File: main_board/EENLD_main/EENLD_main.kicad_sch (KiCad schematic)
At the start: 17 parts, among them J101 Conn_01x06_Pin, J102 Conn_01x02_Pin, SW101 SW_Push, SW102 SW_SPDT, U101 Pico, U102 74HC595, U103 D198K

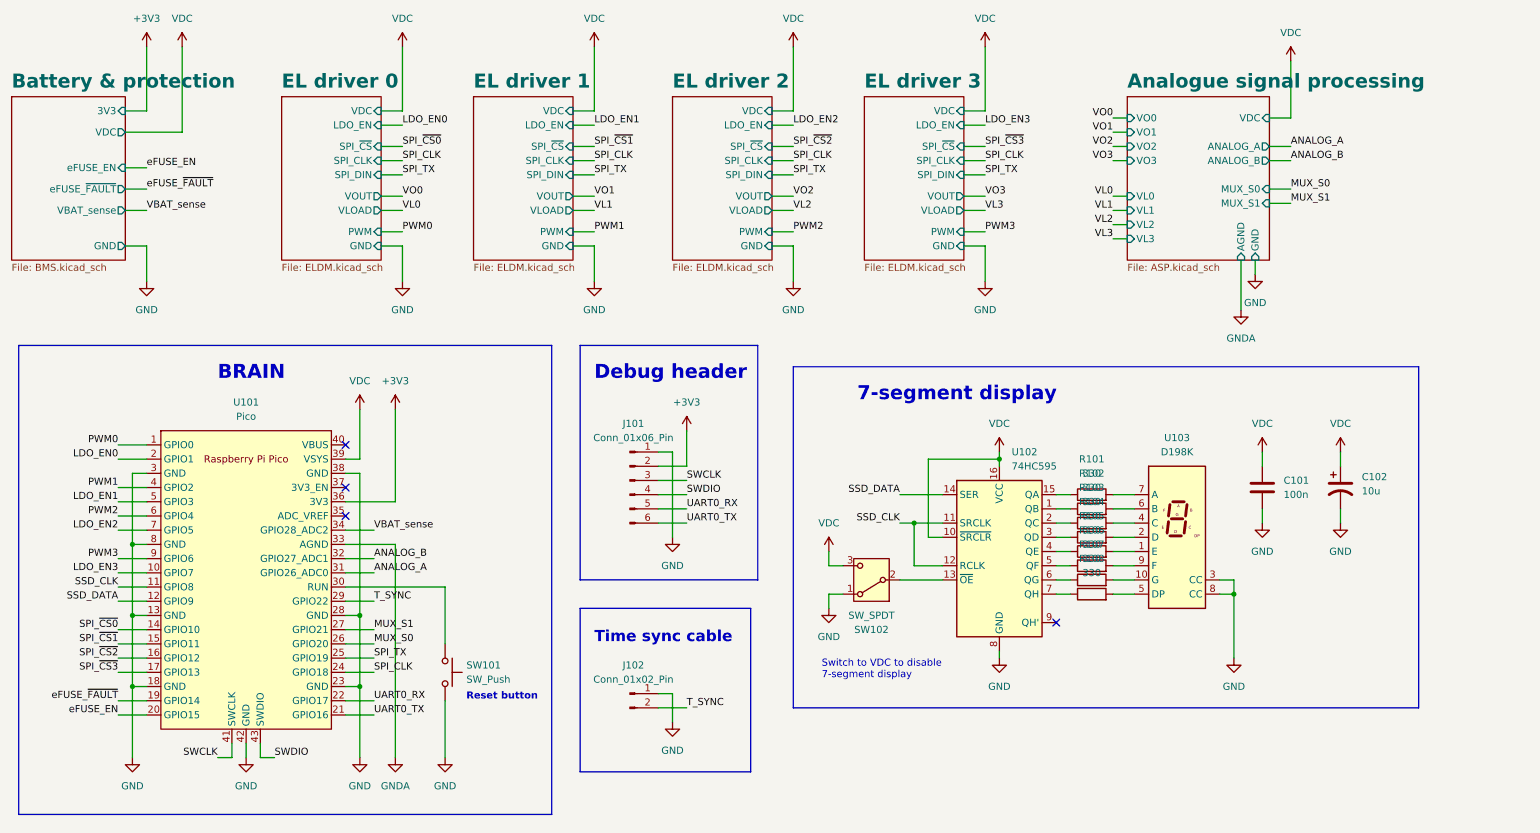
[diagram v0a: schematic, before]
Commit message: Finished PCB layout v0.1.
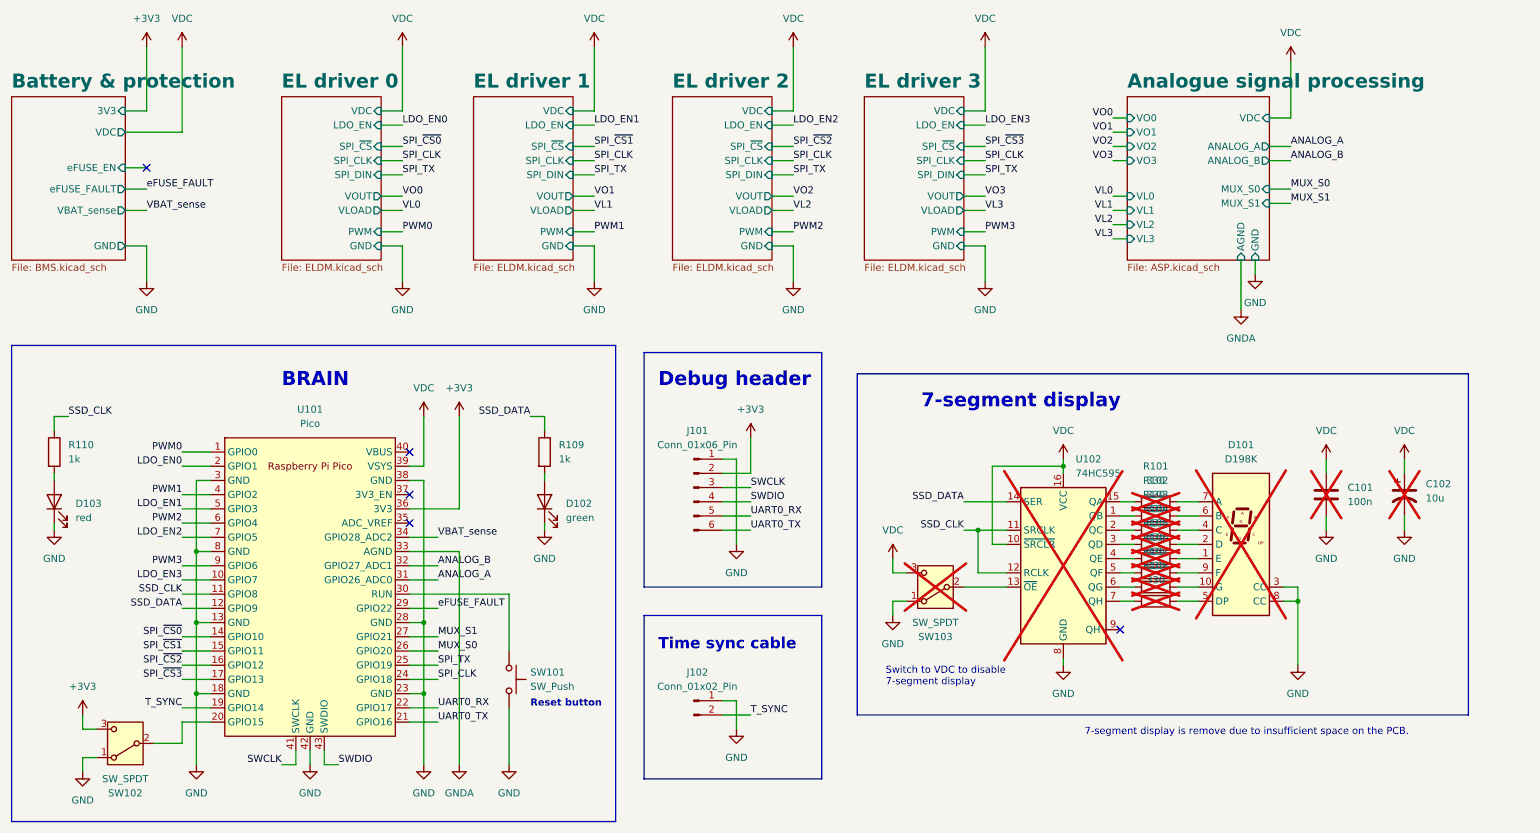
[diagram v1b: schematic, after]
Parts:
- added D102: green, LED_SMD:LED_0805_2012Metric_Pad1.15x1.40mm_HandSolder, symbol Device:LED
- added D103: red, LED_SMD:LED_0805_2012Metric_Pad1.15x1.40mm_HandSolder, symbol Device:LED
- added R109, R110: 1k, Resistor_SMD:R_0603_1608Metric_Pad0.98x0.95mm_HandSolder, symbol Device:R
- added SW102: SW_SPDT, Button_Switch_THT:SW_CK_JS202011CQN_DPDT_Straight, symbol Switch:SW_SPDT
- C101: footprint (none) -> Capacitor_SMD:C_0603_1608Metric_Pad1.08x0.95mm_HandSolder; LCSC (none) -> C14663; now not fitted; now left out of the parts list
- C102: footprint (none) -> Capacitor_THT:CP_Radial_D8.0mm_P2.50mm; now not fitted; now left out of the parts list
- D101: renamed from U103; now not fitted; now left out of the parts list
- J101: footprint (none) -> Connector_PinHeader_2.54mm:PinHeader_1x06_P2.54mm_Vertical
- J102: footprint (none) -> Connector_PinHeader_2.54mm:PinHeader_1x02_P2.54mm_Vertical
- R101, R102, R103, R104, R105, R106, R107, R108: footprint (none) -> Resistor_SMD:R_0603_1608Metric_Pad0.98x0.95mm_HandSolder; LCSC (none) -> C23138; now not fitted; now left out of the parts list
- SW101: footprint Button_Switch_THT:SW_PUSH_6mm -> Button_Switch_SMD:SW_Push_1P1T_NO_6x6mm_H9.5mm
- SW103: renamed from SW102; footprint (none) -> Button_Switch_THT:SW_CK_JS202011CQN_DPDT_Straight; now not fitted; now left out of the parts list
- U101: footprint RPi_Pico:RPi_Pico_SMD_TH -> More Pi Pico:RaspberryPi_Pico_Original_SMD
- U102: LCSC (none) -> C5947; now not fitted; now left out of the parts list
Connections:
- net eFUSE_~{FAULT} is gone; now on net T_SYNC: U101.19 (GPIO14)
- net +3V3: now also SW102.3 (C)
- net GND: now also D102.1 (K), D103.1 (K), SW102.1 (A)
- net SSD_CLK: now also R110.1
- net SSD_DATA: now also R109.1
- net T_SYNC: no longer U101.29 (GPIO22)
- net eFUSE_EN: no longer names the net of U101.20 (GPIO15)
- net eFUSE_EN: now also SW102.2 (B)
- new net: D102.2 (A), R109.2
- new net: D103.2 (A), R110.2
- new net eFUSE_FAULT: U101.29 (GPIO22)
- no-connect marks 4 -> 5
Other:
- sheet Battery & protection ports: added eFUSE_FAULT; removed eFUSE_~{FAULT}
- note added: "7-segment display is remove due to insufficient space on the PCB."
- moved on the sheet: J101, J102, SW101, U101

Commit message: added midi2array
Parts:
- J101, J102, SW101, SW102, U101: now left out of the parts list
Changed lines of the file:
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@@
   )
   (symbol (lib_id "Switch:SW_Push") (at 107.95 135.89 270) (unit 1)
-    (in_bom yes) (on_board yes) (dnp no) (fields_autoplaced)
+    (in_bom no) (on_board yes) (dnp no) (fields_autoplaced)
     (property "Reference" "SW101" (at 111.76 134.62 90)
       (effects (font (size 1.27 1.27)) (justify left))
@@
   )
   (symbol (lib_id "Switch:SW_SPDT") (at 39.37 147.32 180) (unit 1)
-    (in_bom yes) (on_board yes) (dnp no)
+    (in_bom no) (on_board yes) (dnp no)
     (property "Reference" "SW102" (at 39.37 156.21 0)
       (effects (font (size 1.27 1.27)))
@@
   )
   (symbol (lib_id "Connector:Conn_01x02_Pin") (at 140.97 139.7 0) (unit 1)
-    (in_bom yes) (on_board yes) (dnp no) (fields_autoplaced)
+    (in_bom no) (on_board yes) (dnp no) (fields_autoplaced)
     (property "Reference" "J102" (at 141.605 134.62 0)
       (effects (font (size 1.27 1.27)))
@@
   )
   (symbol (lib_id "Connector:Conn_01x06_Pin") (at 140.97 101.6 0) (unit 1)
-    (in_bom yes) (on_board yes) (dnp no) (fields_autoplaced)
+    (in_bom no) (on_board yes) (dnp no) (fields_autoplaced)
     (property "Reference" "J101" (at 141.605 91.44 0)
       (effects (font (size 1.27 1.27)))
@@
   )
   (symbol (lib_id "Pi Pico:Pico") (at 72.39 119.38 0) (unit 1)
-    (in_bom yes) (on_board yes) (dnp no) (fields_autoplaced)
+    (in_bom no) (on_board yes) (dnp no) (fields_autoplaced)
     (property "Reference" "U101" (at 72.39 87.63 0)
       (effects (font (size 1.27 1.27)))
